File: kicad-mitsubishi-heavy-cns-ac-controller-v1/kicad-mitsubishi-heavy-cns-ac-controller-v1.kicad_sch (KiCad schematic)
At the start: 31 parts, among them J3 USB_OTG, J4 Conn_01x05_Pin, SW1 SW_Push, SW2 SW_Push, U1 Si8641BB-B-IU, U2 AP2112K-3.3, U3 ESP32-C3-WROOM-02, U5 AOZ1282CI-1

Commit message: Add input capacitor, add text for cns
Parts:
- C2: footprint Capacitor_Tantalum_SMD:CP_EIA-3528-12_Kemet-T_Pad1.50x2.35mm_HandSolder -> Capacitor_Tantalum_SMD:CP_EIA-3528-12_Kemet-T_HandSolder
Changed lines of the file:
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@@
 			)
 		)
-		(property "Footprint" "Capacitor_Tantalum_SMD:CP_EIA-3528-12_Kemet-T_Pad1.50x2.35mm_HandSolder"
+		(property "Footprint" "Capacitor_Tantalum_SMD:CP_EIA-3528-12_Kemet-T_HandSolder"
 			(at 130.81 49.53 0)
 			(effects

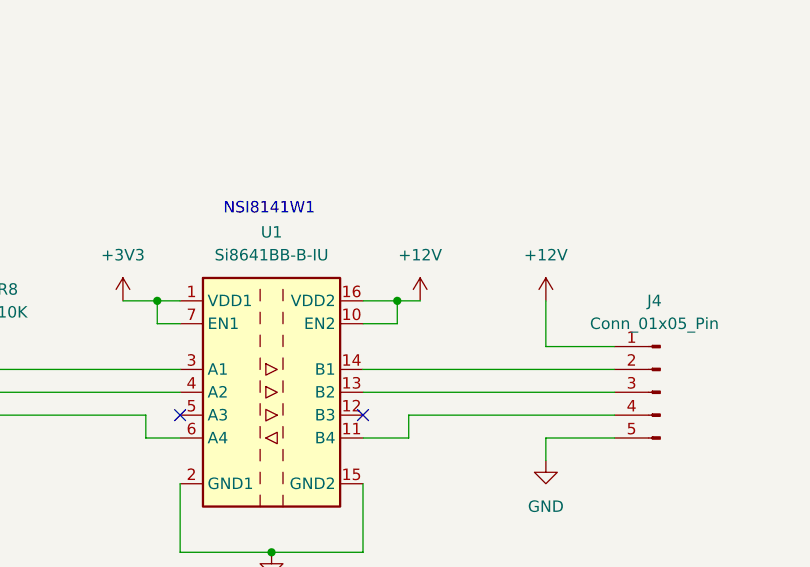
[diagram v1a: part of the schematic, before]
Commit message: Fix digital isolator to be tied to 5v not 12v
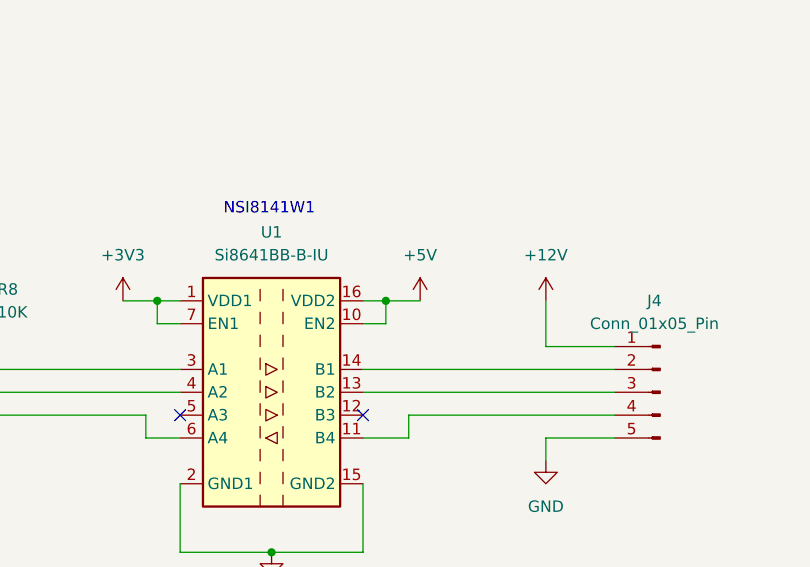
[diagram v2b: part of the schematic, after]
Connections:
- net +12V: no longer U1.10 (EN2), U1.16 (VDD2)
- net +5V: now also U1.10 (EN2), U1.16 (VDD2)
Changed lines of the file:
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@@
 	)
 	(junction
-		(at 74.93 176.53)
+		(at 198.12 96.52)
 		(diameter 0)
 		(color 0 0 0 0)
 	)
 	(junction
-		(at 185.42 124.46)
+		(at 74.93 176.53)
 		(diameter 0)
 		(color 0 0 0 0)
 	)
 	(junction
-		(at 199.39 96.52)
+		(at 185.42 124.46)
 		(diameter 0)
 		(color 0 0 0 0)
@@
 	(wire
 		(pts
-			(xy 199.39 96.52) (xy 201.93 96.52)
-		)
-		(stroke
-			(width 0)
-			(type default)
-		)
-	)
-	(wire
-		(pts
 			(xy 120.65 88.9) (xy 125.73 88.9)
 		)
@@
 	(wire
 		(pts
-			(xy 195.58 99.06) (xy 199.39 99.06)
+			(xy 195.58 99.06) (xy 198.12 99.06)
 		)
 		(stroke
@@
 	(wire
 		(pts
+			(xy 198.12 96.52) (xy 201.93 96.52)
+		)
+		(stroke
+			(width 0)
+			(type default)
+		)
+	)
+	(wire
+		(pts
 			(xy 120.65 106.68) (xy 175.26 106.68)
 		)
@@
 	(wire
 		(pts
-			(xy 199.39 99.06) (xy 199.39 96.52)
+			(xy 198.12 99.06) (xy 198.12 96.52)
 		)
 		(stroke
@@
 	(wire
 		(pts
-			(xy 195.58 96.52) (xy 199.39 96.52)
+			(xy 195.58 96.52) (xy 198.12 96.52)
 		)
 		(stroke
@@
 	)
 	(symbol
+		(lib_id "power:+5V")
+		(at 201.93 96.52 0)
+		(unit 1)
+		(exclude_from_sim no)
+		(in_bom yes)
+		(on_board yes)
+		(dnp no)
+		(fields_autoplaced yes)
+		(property "Reference" "#PWR09"
+			(at 201.93 100.33 0)
+			(effects
+				(font
+					(size 1.27 1.27)
+				)
+				(hide yes)
+			)
+		)
+		(property "Value" "+5V"
+			(at 201.93 91.44 0)
+			(effects
+				(font
+					(size 1.27 1.27)
+				)
+			)
+		)
+		(property "Footprint" ""
+			(at 201.93 96.52 0)
+			(effects
+				(font
+					(size 1.27 1.27)
+				)
+				(hide yes)
+			)
+		)
+		(property "Datasheet" ""
+			(at 201.93 96.52 0)
+			(effects
+				(font
+					(size 1.27 1.27)
+				)
+				(hide yes)
+			)
+		)
+		(property "Description" "Power symbol creates a global label with name \"+5V\""
+			(at 201.93 96.52 0)
+			(effects
+				(font
+					(size 1.27 1.27)
+				)
+				(hide yes)
+			)
+		)
+		(pin "1"
+		)
+		(instances
+			(project "kicad-mitsubishi-heavy-cns-ac-controller-v1"
+				(path "/f7200693-aa8c-4dc9-bbe2-9e962fa196ea"
+					(reference "#PWR09")
+					(unit 1)
+				)
+			)
+		)
+	)
+	(symbol
 		(lib_id "Device:C_Polarized_Small")
 		(at 130.81 49.53 0)
@@
 					(unit 1)
 				)
-			)
-		)
-	)
-	(symbol
-		(lib_id "power:+12V")
-		(at 201.93 96.52 0)
-		(unit 1)
-		(exclude_from_sim no)
-		(in_bom yes)
-		(on_board yes)
-		(dnp no)
-		(property "Reference" "#PWR015"
-			(at 201.93 100.33 0)
-			(effects
-				(font
-					(size 1.27 1.27)
-				)
-				(hide yes)
-			)
-		)
-		(property "Value" "+12V"
-			(at 201.93 91.44 0)
-			(effects
-				(font
-					(size 1.27 1.27)
-				)
-			)
-		)
-		(property "Footprint" ""
-			(at 201.93 96.52 0)
-			(effects
-				(font
-					(size 1.27 1.27)
-				)
-				(hide yes)
-			)
-		)
-		(property "Datasheet" ""
-			(at 201.93 96.52 0)
-			(effects
-				(font
-					(size 1.27 1.27)
-				)
-				(hide yes)
-			)
-		)
-		(property "Description" "Power symbol creates a global label with name \"+12V\""
-			(at 201.93 96.52 0)
-			(effects
-				(font
-					(size 1.27 1.27)
-				)
-				(hide yes)
-			)
-		)
-		(pin "1"
-		)
-		(instances
-			(project "kicad-mitsubishi-heavy-cns-ac-controller-v1"
-				(path "/f7200693-aa8c-4dc9-bbe2-9e962fa196ea"
-					(reference "#PWR015")
-					(unit 1)
-				)

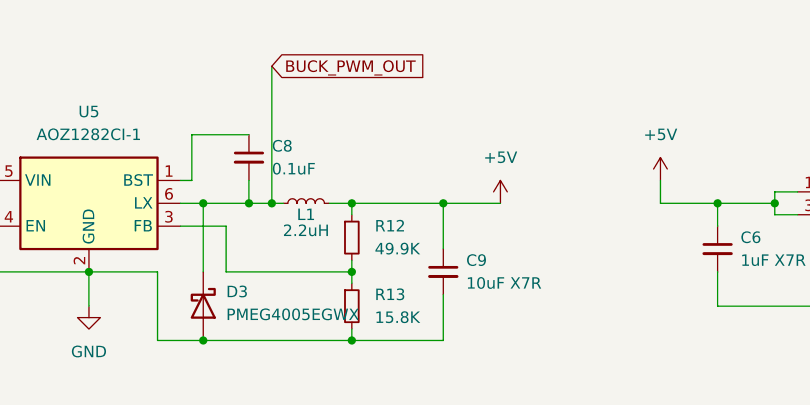
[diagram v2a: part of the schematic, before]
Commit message: Fix 5v to gnd issue. Update resistors for buck converter.
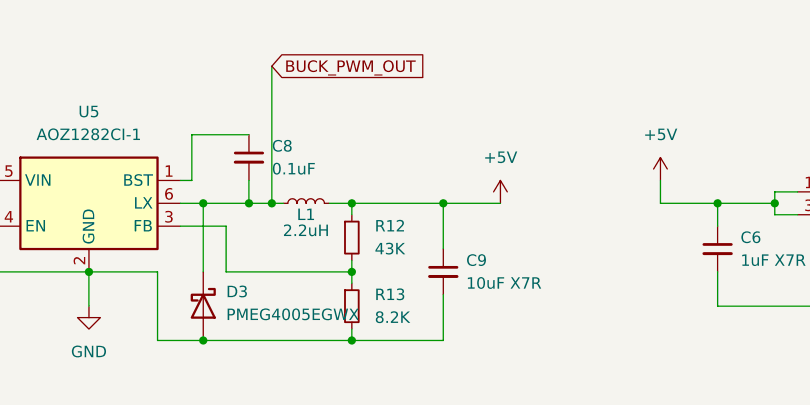
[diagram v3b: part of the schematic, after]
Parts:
- R12: value 49.9K -> 43K
- R13: value 15.8K -> 8.2K
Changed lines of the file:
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@@
 			)
 		)
-		(property "Value" "15.8K"
+		(property "Value" "8.2K"
 			(at 88.9 189.2299 0)
 			(effects
@@
 		(on_board yes)
 		(dnp no)
-		(fields_autoplaced yes)
 		(property "Reference" "R12"
 			(at 88.9 179.0699 0)
@@
 			)
 		)
-		(property "Value" "49.9K"
+		(property "Value" "43K"
 			(at 88.9 181.6099 0)
 			(effects
